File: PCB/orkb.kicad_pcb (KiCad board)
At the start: 2 copper layers, 139.8 x 99.9 mm, 76 parts, among them J1 USB_C_Receptacle_USB2.0, P1 OLED, SW1 MXHS, SW10 MXHS, SW11 MXHS, SW12 MXHS, SW13 MXHS, SW14 MXHS, SW15 MXHS, SW16 MXHS, SW17 MXHS, SW18 MXHS, SW19 MXHS, SW2 MXHS, SW20 MXHS, SW21 MXHS, SW3 MXHS, SW4 MXHS, SW5 MXHS, SW6 MXHS, SW7 MXHS, SW8 MXHS, SW9 MXHS, U1 ProMicro, U2 SRV05-4, U3 SRV05-4

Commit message: Keyboard layout + component placement
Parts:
- JP2: moved to B.Cu
- moved FB2 333.8 mm to (86.7, 92.1), turned to 90 degrees
- moved FB4 333.7 mm to (86.7, 92.1), turned to 90 degrees
- moved JP1 325.1 mm to (103.8, 91.5), turned to -90 degrees
- moved JP2 324.8 mm to (103.8, 91.5), turned to -90 degrees
- moved FB1 323.5 mm to (97.2, 95.9)
- moved FB3 323.3 mm to (97.2, 95.9), turned to 0 degrees
- moved P1 315.1 mm to (96.2, 73.7), turned to -90 degrees
- moved RES2 305.5 mm to (110.7, 56.1)
- moved RES1 305.0 mm to (110.7, 56.1)
- moved D1 4.03 mm to (122.6, 57.2)
- moved D22 4.03 mm to (122.6, 57.2)
- moved U1 1.50 mm to (96.2, 72.8)
- moved U2 1.43 mm to (97.2, 99.9)
- moved U3 1.43 mm to (97.2, 99.9)
- moved J1 1.20 mm to (85.5, 100.2)
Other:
- outline, holes or cut-outs redrawn

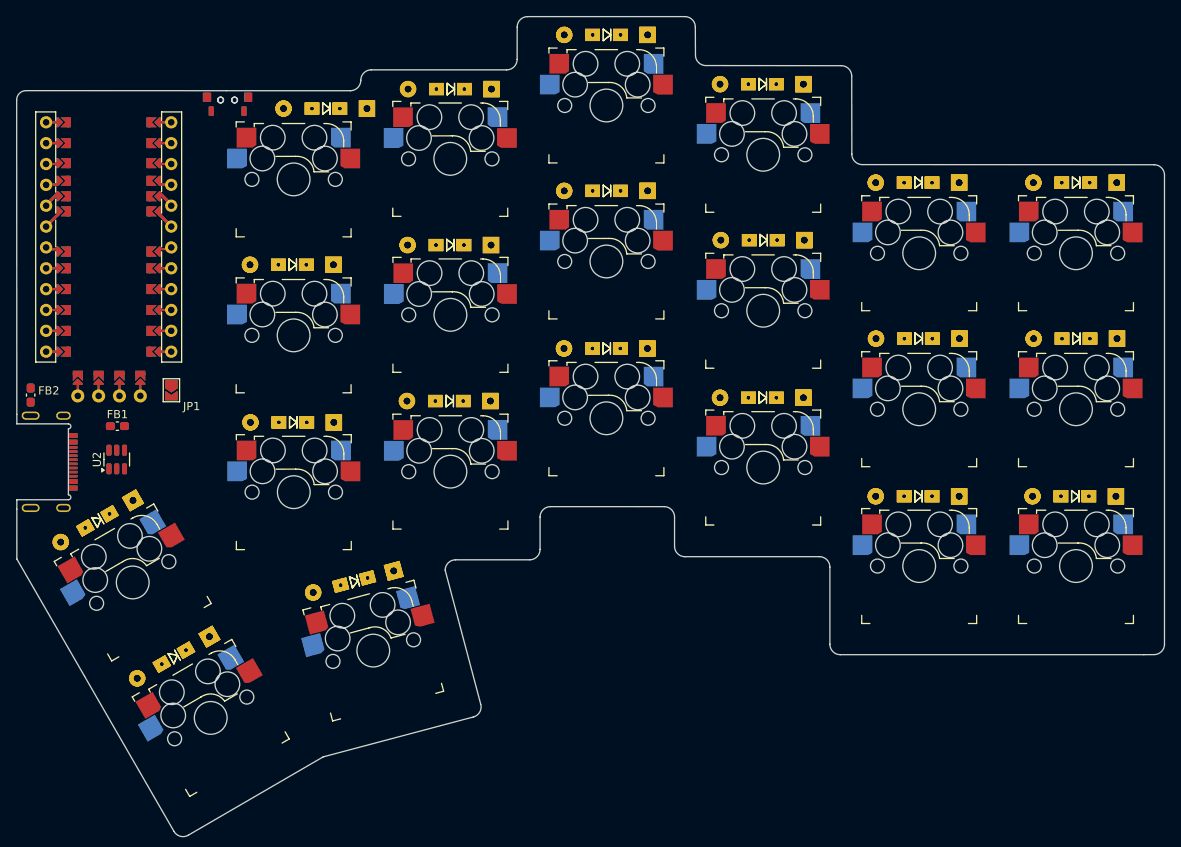
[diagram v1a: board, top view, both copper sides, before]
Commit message: First draft of routing of rows and columns
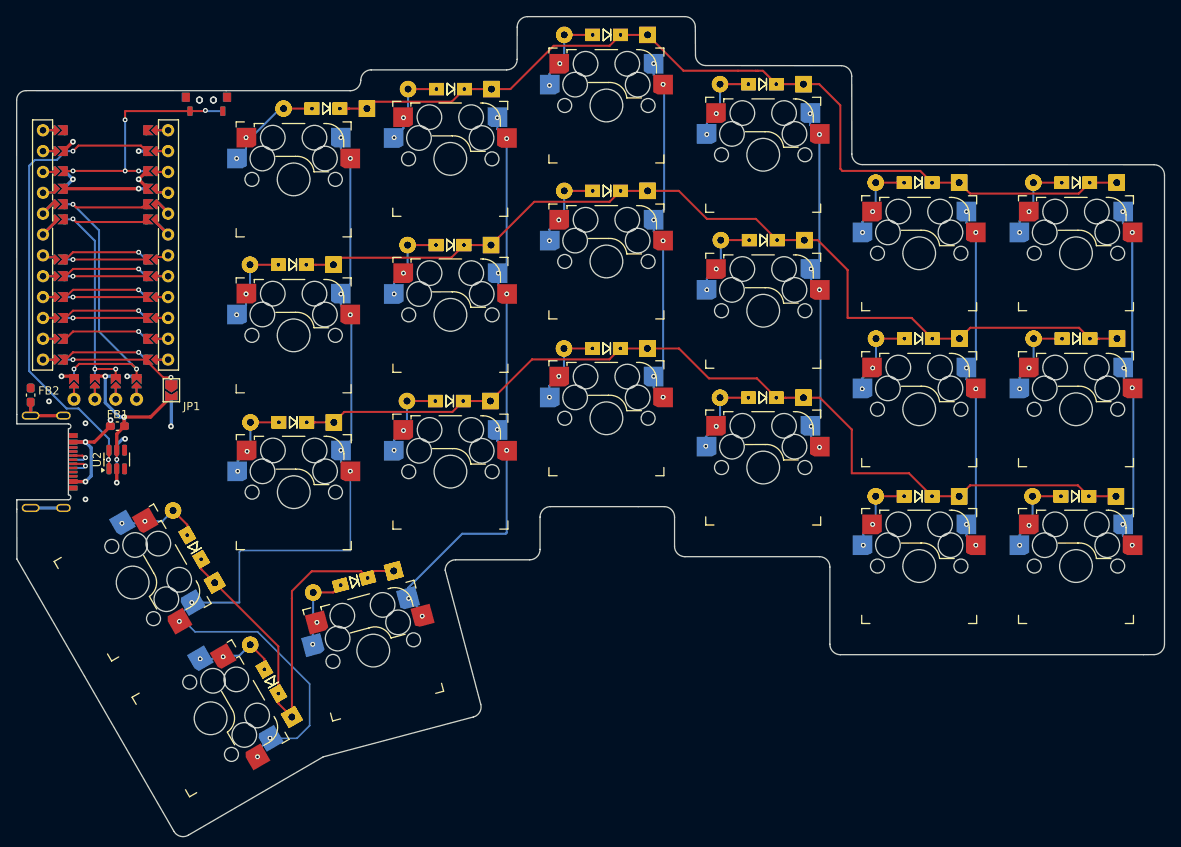
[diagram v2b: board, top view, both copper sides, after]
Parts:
- moved D20 12.2 mm to (116.0, 127.0), turned to 120 degrees
- moved D41 12.2 mm to (116.0, 127.0), turned to 120 degrees
- moved D19 12.2 mm to (106.6, 110.6), turned to 120 degrees
- moved D40 12.2 mm to (106.6, 110.6), turned to 120 degrees
- moved RES1 2.58 mm to (108.1, 56.1)
- moved RES2 2.58 mm to (108.1, 56.1)
- moved U1 1.04 mm to (95.8, 73.8)
- moved P1 0.61 mm to (95.8, 74.1)
- turned SW20 to 120 degrees
- turned SW19 to 120 degrees
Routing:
- net row1: track 0.00 -> 124.2 mm, vias 0 -> 1
- net col0: track 0.00 -> 124.1 mm, vias 0 -> 11
- net row2: track 0.00 -> 123.7 mm, vias 0 -> 1
- net row0: track 0.00 -> 121.2 mm, vias 0 -> 1
- net col1: track 0.00 -> 82.2 mm, vias 0 -> 9
- net DATA: track 0.00 -> 66.4 mm, vias 0 -> 4
- net row3: track 0.00 -> 62.9 mm, vias 0 -> 1
- net col2: track 0.00 -> 53.6 mm, vias 0 -> 7
- net col4: track 0.00 -> 53.5 mm, vias 0 -> 7
- net col5: track 0.00 -> 53.5 mm, vias 0 -> 7
- net col3: track 0.00 -> 53.4 mm, vias 0 -> 7
- net SDA: track 0.00 -> 43.2 mm, vias 0 -> 3
- net SCL: track 0.00 -> 33.7 mm, vias 0 -> 3
- net VCC: track 0.00 -> 33.2 mm, vias 0 -> 4
- net RESET: track 0.00 -> 29.1 mm, vias 0 -> 5
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
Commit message: Refactoring entire project
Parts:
- added D43: 1N4841/1N4148W, SplitKeyboard_Common:Diode_DO35_SOD123_Hybrid, F.Cu at (114.8, 109.7)
- added D44: 1N4841/1N4148W, SplitKeyboard_Common:Diode_DO35_SOD123_Hybrid, F.Cu at (138.4, 106.6)
- added SW22: MXHS, SplitKeyboard_Common:SW_MX_HotSwap_Reversible, B.Cu at (138.4, 115.2)
- D1, D10, D11, D12, D13, D14, D15, D16, D17, D18, D19, D2, D20, D21, D23, D24, D25, D26, D27, D28, D29, D3, D30, D31, D32, D33, D34, D35, D36, D37, D38, D39, D4, D40, D41, D42, D5, D6, D7, D8, D9: value 1N4148/1N4148W -> 1N4841/1N4148W
- D22: value 1N4148/1N4148W -> 1N4841/1N4148W; moved to B.Cu
- JP1, JP2: value Jumper_2 -> Jumper_2_Open; footprint Jumper:SolderJumper-2_P1.3mm_Open_TrianglePad1.0x1.5mm -> SplitKeyboard_Common:Jumper_min_v2
- P1: moved to B.Cu
- moved D40 97.0 mm to (202.9, 99.1), turned to 180 degrees
- moved D28 85.8 mm to (202.9, 61.0)
- moved D34 85.7 mm to (202.9, 80.0)
- moved D22 51.8 mm to (138.4, 106.6)
- moved D41 42.0 mm to (74.5, 133.1), turned to -135 degrees
- moved D19 39.2 mm to (74.5, 133.1), turned to -135 degrees
- moved D32 34.6 mm to (164.8, 67.9)
- moved D26 34.6 mm to (164.8, 48.9)
- moved D38 34.5 mm to (165.0, 87.0)
- moved D42 33.1 mm to (93.2, 118.7), turned to -150 degrees
- moved D31 32.1 mm to (145.8, 62.0)
- moved D37 32.1 mm to (145.8, 81.0)
- moved D25 32.1 mm to (145.8, 42.9)
- moved SW19 30.6 mm to (80.6, 139.3), turned to -135 degrees
- moved D33 30.5 mm to (183.9, 80.0)
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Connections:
- D22 pad 1: row0 -> row3
- D22 pad 2: Net-(D1-A) -> Net-(D22-A)
- D23 pad 2: Net-(D2-A) -> Net-(D1-A)
- D24 pad 2: Net-(D24-A) -> Net-(D2-A)
- D28 pad 1: row1 -> row0
- D3 pad 2: Net-(D24-A) -> Net-(D25-A)
- D31 pad 2: Net-(D10-A) -> Net-(D31-A)
- D32 pad 2: Net-(D11-A) -> Net-(D10-A)
- D33 pad 2: Net-(D12-A) -> Net-(D11-A)
- D34 pad 1: row2 -> row1
- D34 pad 2: Net-(D13-A) -> Net-(D12-A)
- D35 pad 2: Net-(D14-A) -> Net-(D13-A)
- D36 pad 2: Net-(D15-A) -> Net-(D14-A)
- D37 pad 2: Net-(D16-A) -> Net-(D15-A)
- D38 pad 2: Net-(D17-A) -> Net-(D16-A)
- D39 pad 2: Net-(D18-A) -> Net-(D17-A)
- D4 pad 2: Net-(D25-A) -> Net-(D26-A)
- D40 pad 1: row3 -> row2
- D40 pad 2: Net-(D19-A) -> Net-(D18-A)
- D41 pad 2: Net-(D20-A) -> Net-(D19-A)
- D42 pad 2: Net-(D21-A) -> Net-(D20-A)
- D5 pad 2: Net-(D26-A) -> Net-(D27-A)
- D6 pad 2: Net-(D27-A) -> Net-(D28-A)
- D7 pad 2: Net-(D28-A) -> Net-(D29-A)
- D8 pad 2: Net-(D29-A) -> Net-(D30-A)
- D9 pad 2: Net-(D30-A) -> Net-(D31-A)
- SW20 pad 1: col0 -> col1
- SW21 pad 1: col1 -> col2
- SW3 pad 2: Net-(D24-A) -> Net-(D25-A)
- SW4 pad 2: Net-(D25-A) -> Net-(D26-A)
- SW5 pad 2: Net-(D26-A) -> Net-(D27-A)
- SW6 pad 2: Net-(D27-A) -> Net-(D28-A)
- SW7 pad 2: Net-(D28-A) -> Net-(D29-A)
- SW8 pad 2: Net-(D29-A) -> Net-(D30-A)
- SW9 pad 2: Net-(D30-A) -> Net-(D31-A)
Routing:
- net row1: track 124.2 -> 0.00 mm, vias 1 -> 0
- net col0: track 124.1 -> 0.00 mm, vias 11 -> 0
- net row2: track 123.7 -> 0.00 mm, vias 1 -> 0
- net row0: track 121.2 -> 0.00 mm, vias 1 -> 0
- net col1: track 82.2 -> 0.00 mm, vias 9 -> 0
- net DATA: track 66.4 -> 0.00 mm, vias 4 -> 0
- net row3: track 62.9 -> 0.00 mm, vias 1 -> 0
- net col2: track 53.6 -> 0.00 mm, vias 7 -> 0
- net col4: track 53.5 -> 0.00 mm, vias 7 -> 0
- net col5: track 53.5 -> 0.00 mm, vias 7 -> 0
- net col3: track 53.4 -> 0.00 mm, vias 7 -> 0
- net SDA: track 43.2 -> 0.00 mm, vias 3 -> 0
- net SCL: track 33.7 -> 0.00 mm, vias 3 -> 0
- net VCC: track 33.2 -> 0.00 mm, vias 4 -> 0
- net RESET: track 29.1 -> 0.00 mm, vias 5 -> 0
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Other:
- board size 139.8 x 99.9 mm -> 304.3 x 117.2 mm

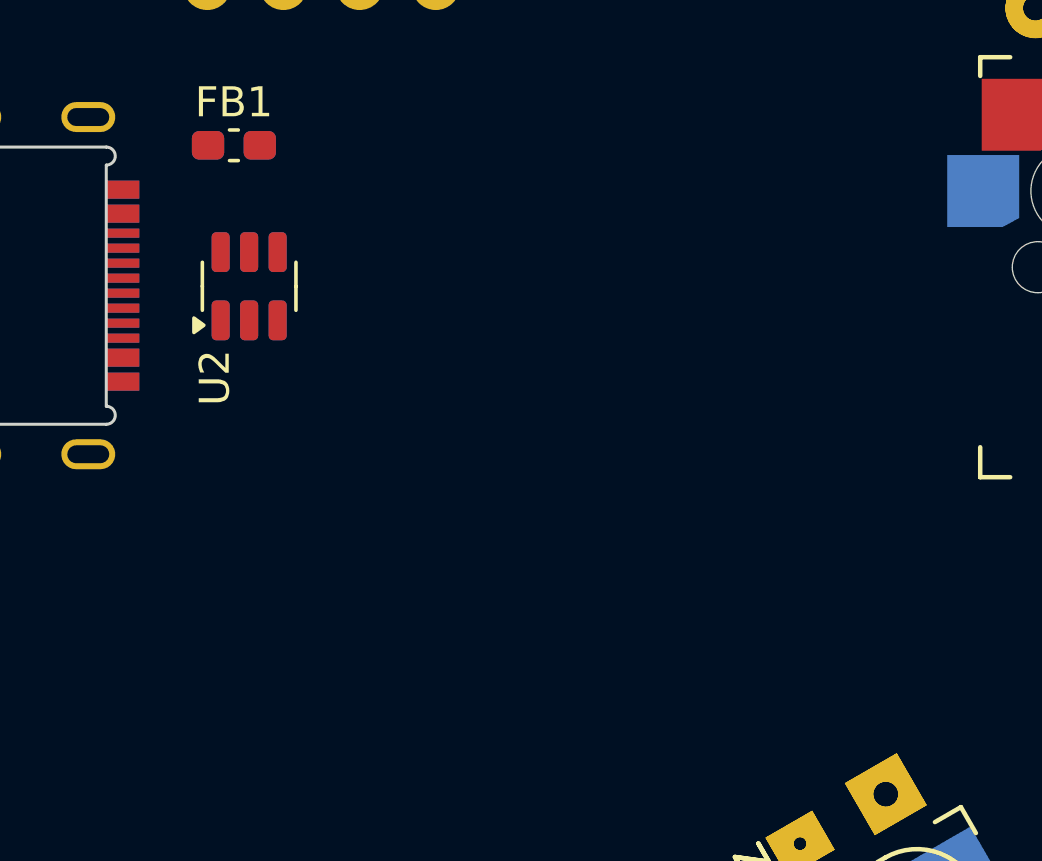
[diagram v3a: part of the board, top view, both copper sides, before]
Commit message: Added extra index finger switch
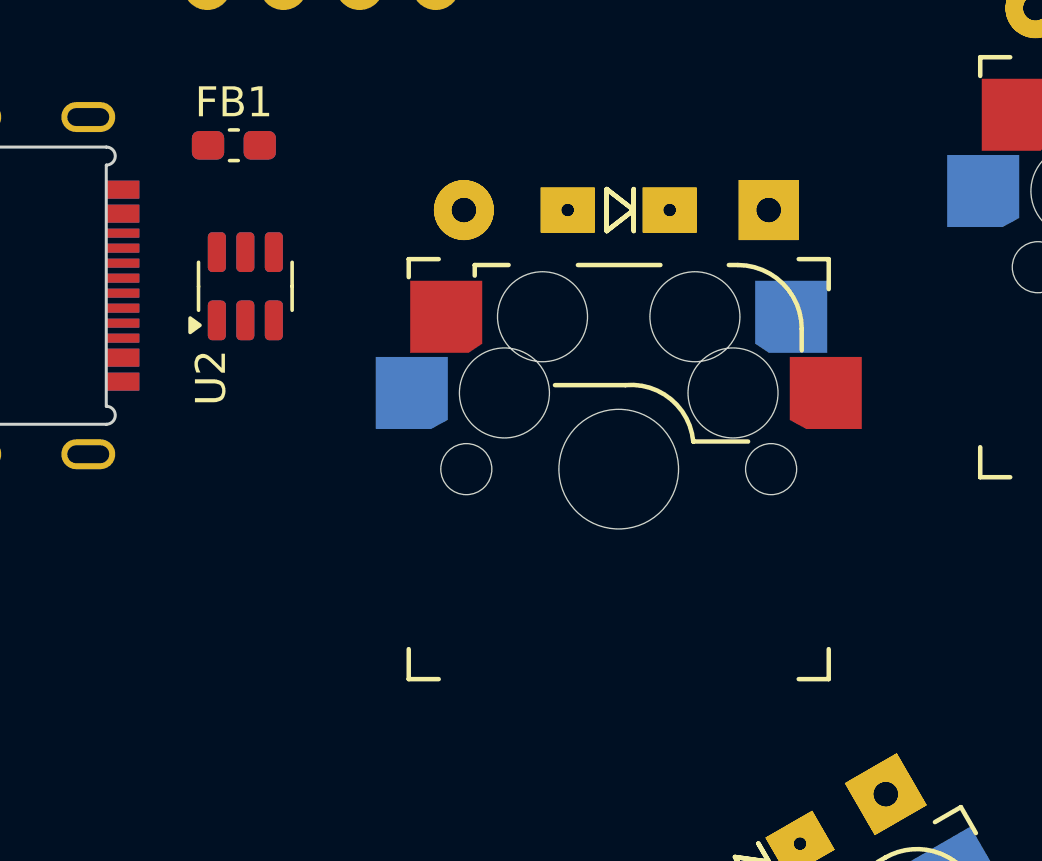
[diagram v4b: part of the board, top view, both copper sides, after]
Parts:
- added D45: 1N4841/1N4148W, SplitKeyboard_Common:Diode_DO35_SOD123_Hybrid, B.Cu at (88.6, 96.8)
- added D46: 1N4841/1N4148W, SplitKeyboard_Common:Diode_DO35_SOD123_Hybrid, F.Cu at (88.6, 96.8)
- added SW23: MXHS, SplitKeyboard_Common:SW_MX_HotSwap_Reversible, F.Cu at (88.6, 105.4)
- moved U2 0.13 mm to (76.2, 99.3)
- moved U3 0.13 mm to (76.2, 99.3)
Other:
- board text added: "ENCODER HERE"
